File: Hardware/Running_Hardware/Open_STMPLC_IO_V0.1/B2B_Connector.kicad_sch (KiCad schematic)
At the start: 6 parts, among them J39 10144517-041802LF, J41 10144517-041802LF, J42 10144517-041802LF, J43 Screw_Terminal_01x02

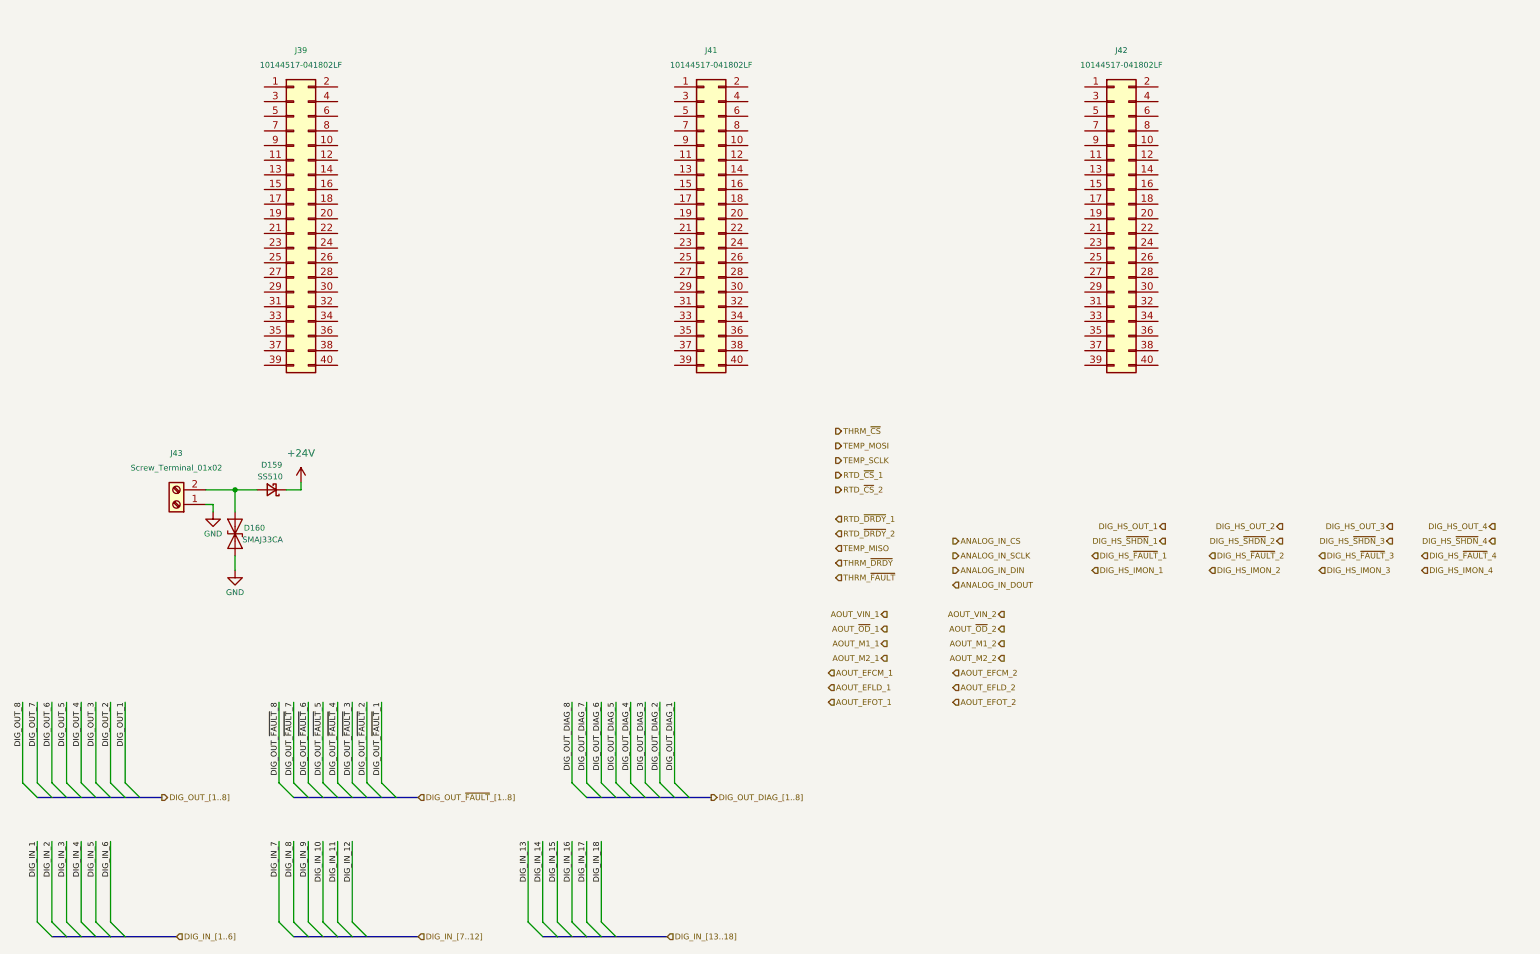
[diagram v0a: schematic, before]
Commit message: Common GND terminal changes
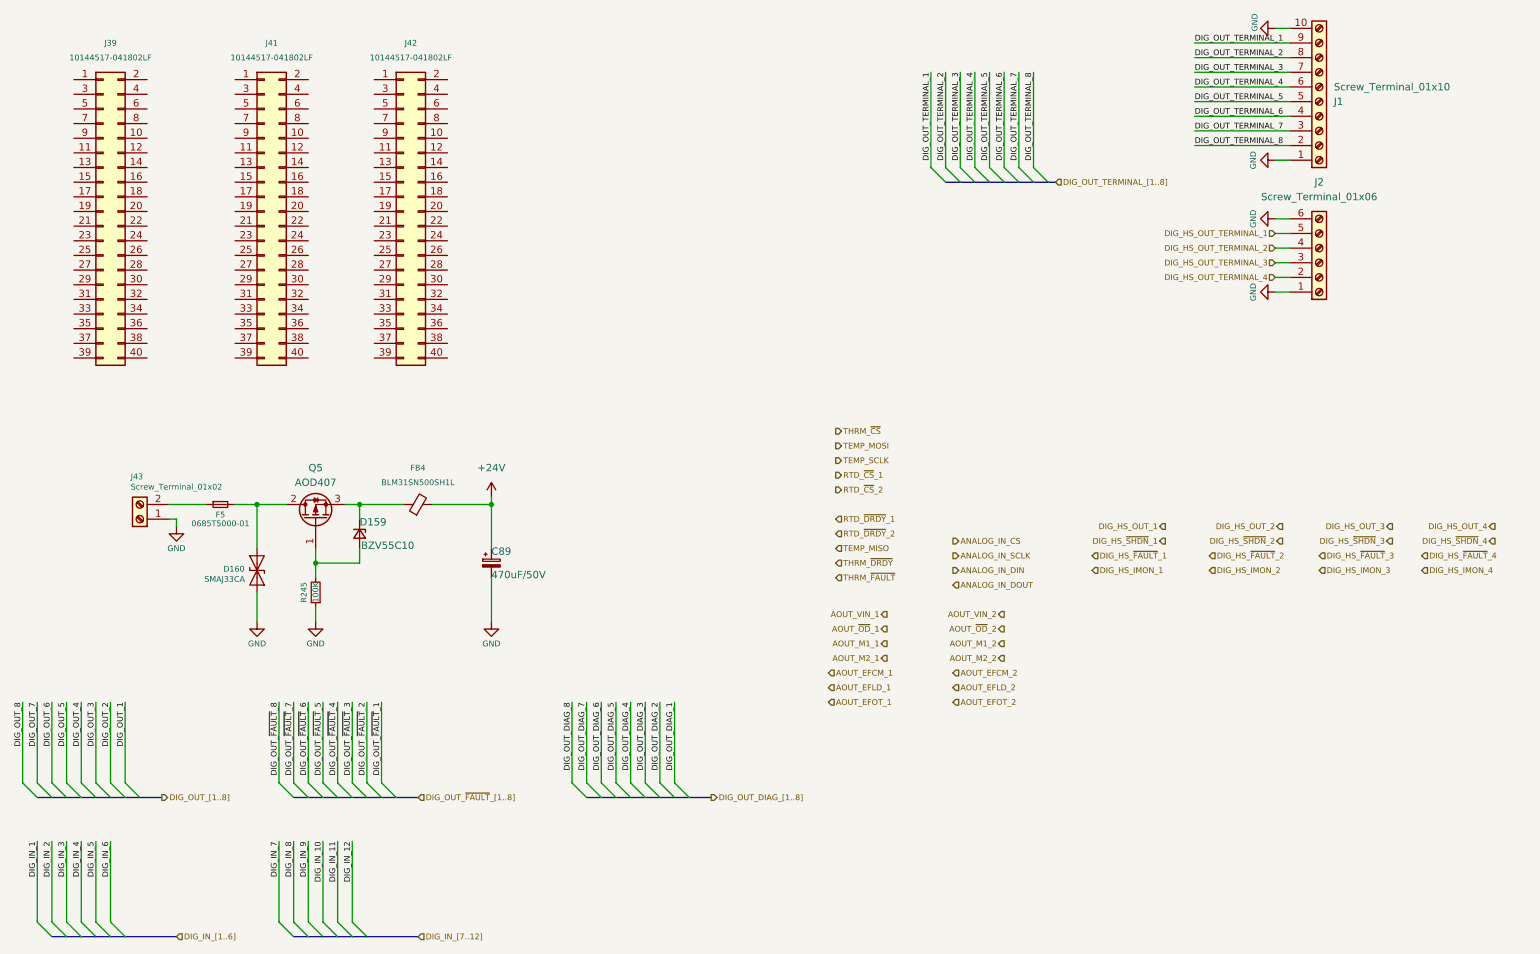
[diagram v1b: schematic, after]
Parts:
- removed D159: SS510, Diode_SMD:D_SMA, symbol Device:D_Schottky_Small
- added C89: 470uF/50V, Capacitor_THT:CP_Radial_D10.0mm_P5.00mm, symbol Device:C_Polarized_Small
- added D159: BZV55C10, Diode_SMD:D_MiniMELF, symbol Device:D_Zener_Small
- added F5: 0685T5000-01, Fuse:Fuse_1206_3216Metric, symbol Device:Fuse_Small
- added FB4: BLM31SN500SH1L, Inductor_SMD:L_1206_3216Metric_Pad1.22x1.90mm_HandSolder, symbol Device:FerriteBead_Small
- added J1: Screw_Terminal_01x10, TerminalBlock_Phoenix:TerminalBlock_Phoenix_MKDS-1-10-3.81_1x10_P3.81mm_Horizontal, symbol Connector:Screw_Terminal_01x10
- added J2: Screw_Terminal_01x06, TerminalBlock_Phoenix:TerminalBlock_Phoenix_MKDS-1-6-3.81_1x06_P3.81mm_Horizontal, symbol Connector:Screw_Terminal_01x06
- added Q5: AOD407, Package_TO_SOT_SMD:TO-252-3_TabPin2, symbol Transistor_FET:Q_PMOS_GDS
- added R245: 100K, Resistor_SMD:R_0603_1608Metric_Pad0.98x0.95mm_HandSolder, symbol Device:R_Small
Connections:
- net +24V: now also C89.1, FB4.2
- net GND: now also C89.2, J1.1 (Pin_1), J1.10 (Pin_10), J2.1 (Pin_1), J2.6 (Pin_6), R245.1
- net at J43.2 (Pin_2): now also F5.1; no longer D160.1 (A1)
- new net: D160.1 (A1), F5.2, Q5.2 (D)
- new net: D159.2 (A), Q5.1 (G), R245.2
- new net: D159.1 (K), FB4.1, Q5.3 (S)
- new net DIG_HS_OUT_TERMINAL_1: J2.5 (Pin_5)
- new net DIG_HS_OUT_TERMINAL_2: J2.4 (Pin_4)
- new net DIG_HS_OUT_TERMINAL_3: J2.3 (Pin_3)
- new net DIG_HS_OUT_TERMINAL_4: J2.2 (Pin_2)
- new net DIG_OUT_TERMINAL_1: J1.9 (Pin_9)
- new net DIG_OUT_TERMINAL_2: J1.8 (Pin_8)
- new net DIG_OUT_TERMINAL_3: J1.7 (Pin_7)
- new net DIG_OUT_TERMINAL_4: J1.6 (Pin_6)
- new net DIG_OUT_TERMINAL_5: J1.5 (Pin_5)
- new net DIG_OUT_TERMINAL_6: J1.4 (Pin_4)
- new net DIG_OUT_TERMINAL_7: J1.3 (Pin_3)
- new net DIG_OUT_TERMINAL_8: J1.2 (Pin_2)
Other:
- moved on the sheet: D160, J39, J41, J42, J43

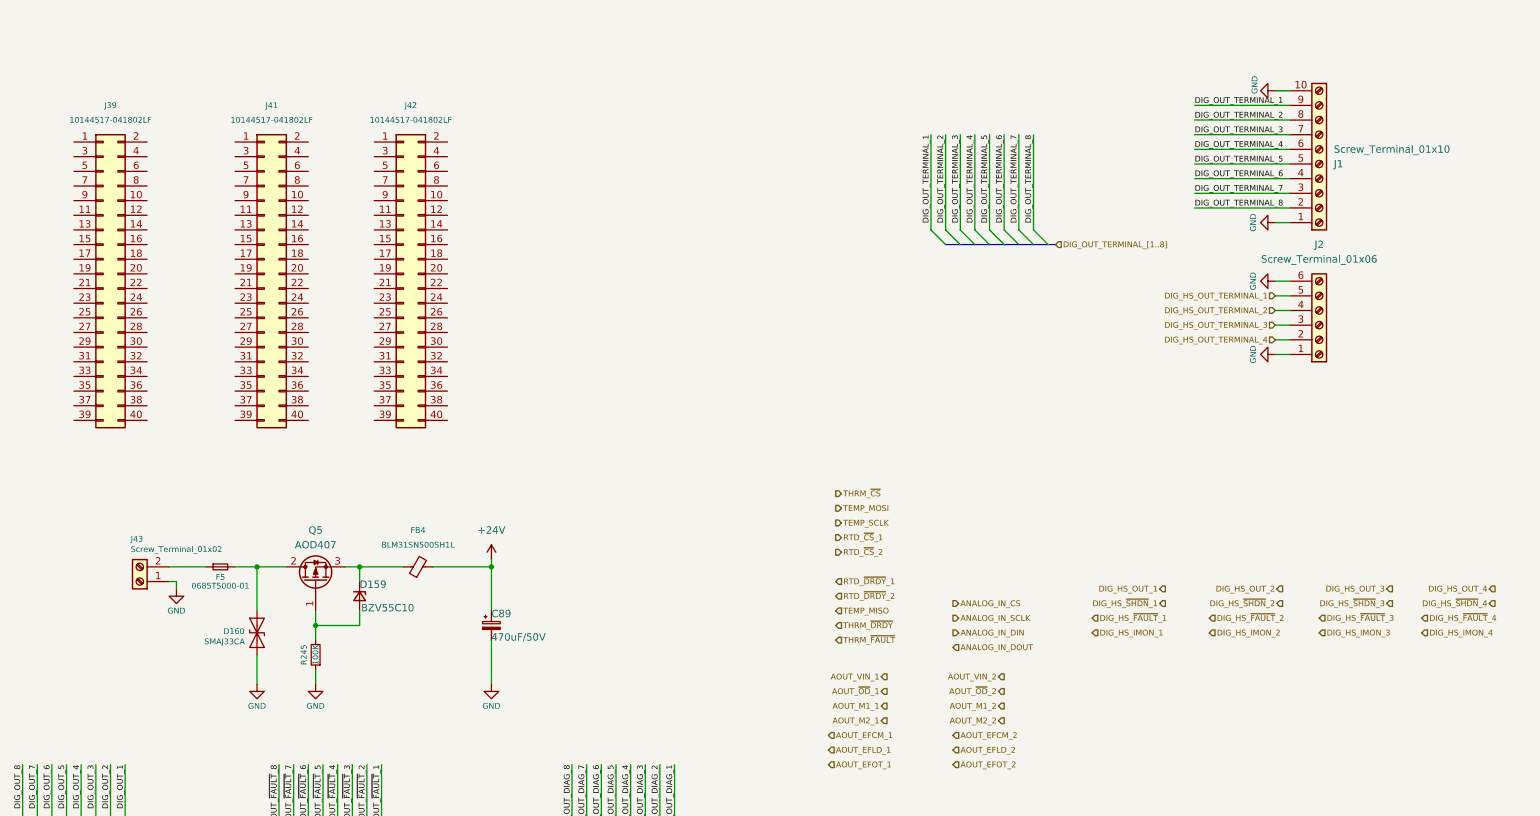
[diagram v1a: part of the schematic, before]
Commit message: Input circuit added
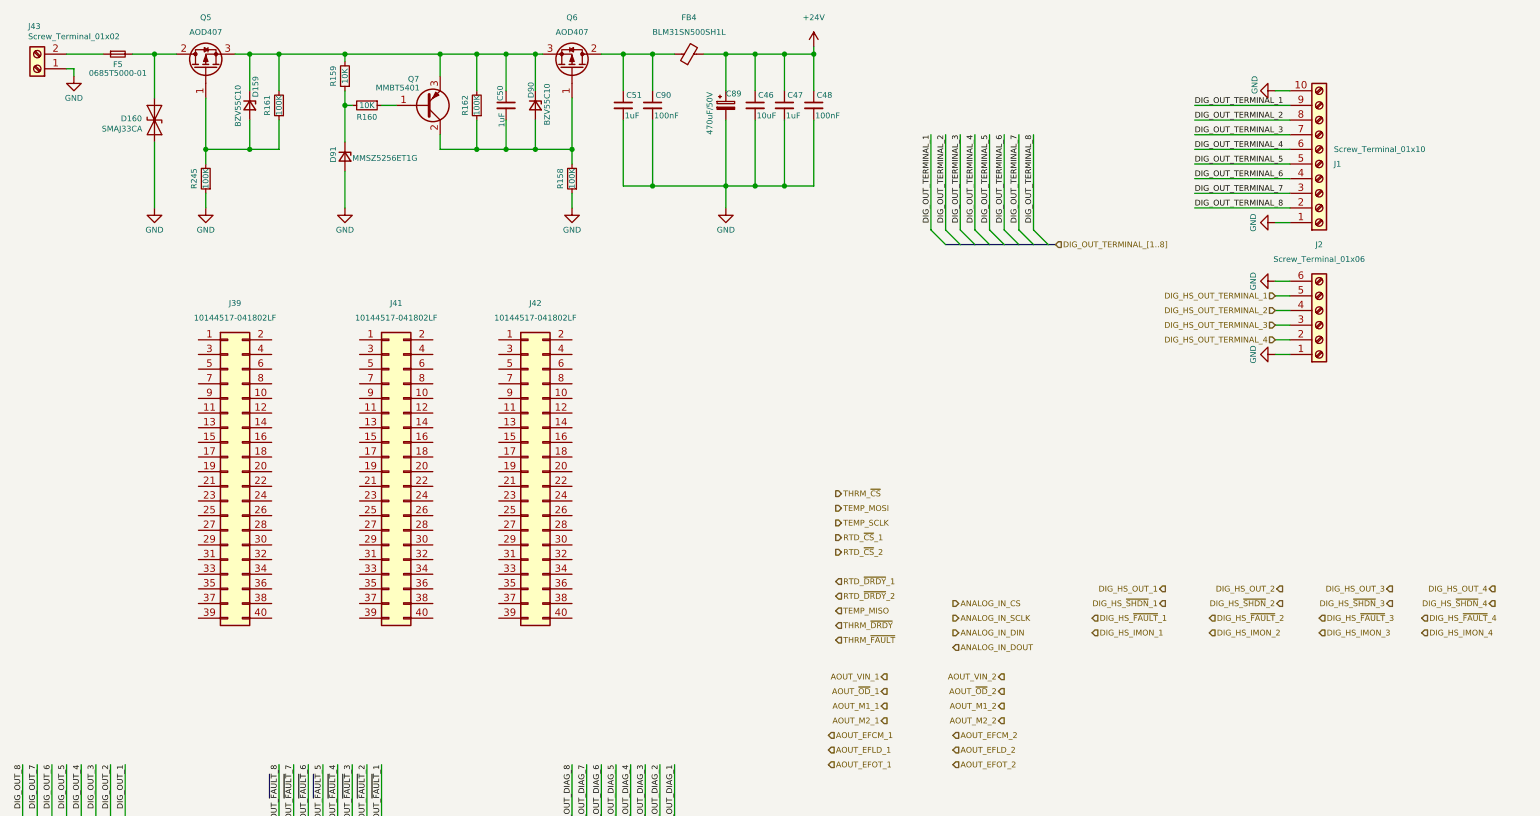
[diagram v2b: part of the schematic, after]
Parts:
- added C46: 10uF, Capacitor_SMD:C_0805_2012Metric_Pad1.18x1.45mm_HandSolder, symbol Device:C_Small
- added C47, C50, C51: 1uF, Capacitor_SMD:C_0603_1608Metric_Pad1.08x0.95mm_HandSolder, symbol Device:C_Small
- added C48, C90: 100nF, Capacitor_SMD:C_0603_1608Metric_Pad1.08x0.95mm_HandSolder, symbol Device:C_Small
- added D90: BZV55C10, Diode_SMD:D_MiniMELF, symbol Device:D_Zener_Small
- added D91: MMSZ5256ET1G, Diode_SMD:D_MiniMELF, symbol Device:D_Zener_Small
- added Q6: AOD407, Package_TO_SOT_SMD:TO-252-3_TabPin2, symbol Transistor_FET:Q_PMOS_GDS
- added Q7: MMBT5401, symbol Transistor_BJT:Q_PNP_BCE
- added R158, R161, R162: 100K, Resistor_SMD:R_0603_1608Metric_Pad0.98x0.95mm_HandSolder, symbol Device:R_Small
- added R159, R160: 10K, Resistor_SMD:R_0603_1608Metric_Pad0.98x0.95mm_HandSolder, symbol Device:R_Small
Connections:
- net +24V: now also C46.1, C47.1, C48.1
- net GND: now also C46.2, C47.2, C48.2, C51.2, C90.2, D91.2 (A), R158.1
- net at D159.2 (A), Q5.1 (G), R245.2: now also R161.1
- net at D159.1 (K), Q5.3 (S): now also C50.1, D90.1 (K), Q6.3 (S), Q7.3 (E), R159.2, R161.2, R162.2; no longer FB4.1
- new net: C51.1, C90.1, FB4.1, Q6.2 (D)
- new net: C50.2, D90.2 (A), Q6.1 (G), Q7.2 (C), R158.2, R162.1
- new net: Q7.1 (B), R160.1
- new net: D91.1 (K), R159.1, R160.2
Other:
- moved on the sheet: C89, D159, D160, F5, FB4, J39, J41, J42, J43, Q5, R245

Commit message: IO board layout
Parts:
- Q7: footprint (none) -> Package_TO_SOT_SMD:SOT-23
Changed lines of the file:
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@@
 			)
 		)
-		(property "Footprint" ""
+		(property "Footprint" "Package_TO_SOT_SMD:SOT-23"
 			(at 91.44 36.83 0)
 			(effects

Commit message: IO board layout 1
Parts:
- C89: value 470uF/50V -> 220uF/50V; footprint Capacitor_THT:CP_Radial_D10.0mm_P5.00mm -> Capacitor_SMD:CP_Elec_10x10.5
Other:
- moved on the sheet: C46, C48
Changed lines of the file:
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@@
 	(symbol
 		(lib_id "Device:C_Small")
-		(at 153.67 34.29 0)
+		(at 143.51 34.29 0)
 		(unit 1)
 		(exclude_from_sim no)
@@
 		(dnp no)
 		(property "Reference" "C48"
-			(at 154.178 32.512 0)
+			(at 144.018 32.512 0)
 			(effects
 				(font
@@
 		)
 		(property "Value" "100nF"
-			(at 153.924 36.068 0)
+			(at 143.764 36.068 0)
 			(effects
 				(font
@@
 		)
 		(property "Footprint" "Capacitor_SMD:C_0603_1608Metric_Pad1.08x0.95mm_HandSolder"
-			(at 153.67 34.29 0)
+			(at 143.51 34.29 0)
 			(effects
 				(font
@@
 		)
 		(property "Datasheet" "~"
-			(at 153.67 34.29 0)
+			(at 143.51 34.29 0)
 			(effects
 				(font
@@
 		)
 		(property "Description" "Unpolarized capacitor, small symbol"
-			(at 153.67 34.29 0)
+			(at 143.51 34.29 0)
 			(effects
 				(font
@@
 			)
 		)
-		(property "Value" "470uF/50V"
+		(property "Value" "220uF/50V"
 			(at 135.636 39.37 90)
 			(effects
@@
 			)
 		)
-		(property "Footprint" "Capacitor_THT:CP_Radial_D10.0mm_P5.00mm"
+		(property "Footprint" "Capacitor_SMD:CP_Elec_10x10.5"
 			(at 138.43 34.29 0)
 			(effects
@@
 	(symbol
 		(lib_id "Device:C_Small")
-		(at 143.51 34.29 0)
+		(at 153.67 34.29 0)
 		(unit 1)
 		(exclude_from_sim no)
@@
 		(dnp no)
 		(property "Reference" "C46"
-			(at 144.018 32.512 0)
+			(at 154.178 32.512 0)
 			(effects
 				(font
@@
 		)
 		(property "Value" "10uF"
-			(at 143.764 36.068 0)
+			(at 153.924 36.068 0)
 			(effects
 				(font
@@
 		)
 		(property "Footprint" "Capacitor_SMD:C_0805_2012Metric_Pad1.18x1.45mm_HandSolder"
-			(at 143.51 34.29 0)
+			(at 153.67 34.29 0)
 			(effects
 				(font
@@
 		)
 		(property "Datasheet" "~"
-			(at 143.51 34.29 0)
+			(at 153.67 34.29 0)
 			(effects
 				(font
@@
 		)
 		(property "Description" "Unpolarized capacitor, small symbol"
-			(at 143.51 34.29 0)
-			(effects
-				(font
+			(at 153.67 34.29 0)
+			(effects
+				(font

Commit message: LED arrengements
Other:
- moved on the sheet: C50, D159, D160, D90, D91, J43, Q7, R159, R160, R161, R162, R245

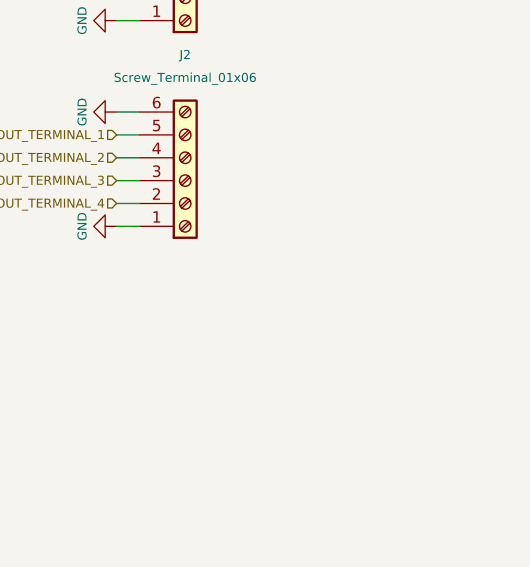
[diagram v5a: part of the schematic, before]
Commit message: Component placement IO board
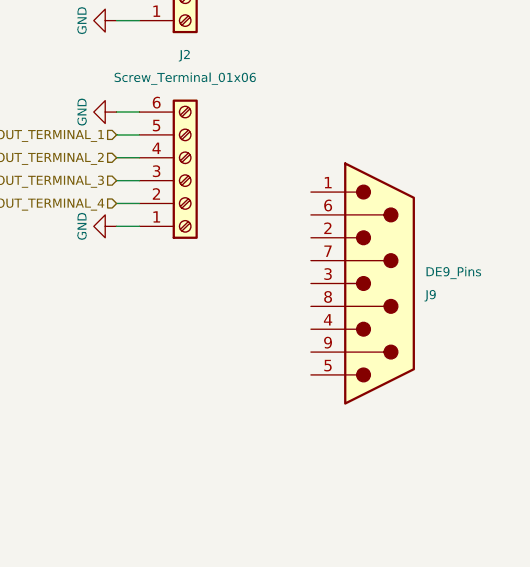
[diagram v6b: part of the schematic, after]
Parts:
- added J9: DE9_Pins, A-DF_09_PP_Z:A-DF_09_PP_Z, symbol Connector:DE9_Pins
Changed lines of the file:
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@@
+	)
+	(symbol
+		(lib_id "Connector:DE9_Pins")
+		(at 262.89 83.82 0)
+		(mirror x)
+		(unit 1)
+		(exclude_from_sim no)
+		(in_bom yes)
+		(on_board yes)
+		(dnp no)
+		(property "Reference" "J9"
+			(at 267.97 85.0901 0)
+			(effects
+				(font
+					(size 1 1)
+				)
+				(justify left)
+			)
+		)
+		(property "Value" "DE9_Pins"
+			(at 267.97 82.5501 0)
+			(effects
+				(font
+					(size 1 1)
+				)
+				(justify left)
+			)
+		)
+		(property "Footprint" "A-DF_09_PP_Z:A-DF_09_PP_Z"
+			(at 262.89 83.82 0)
+			(effects
+				(font
+					(size 1.27 1.27)
+				)
+				(hide yes)
+			)
+		)
+		(property "Datasheet" "~"
+			(at 262.89 83.82 0)
+			(effects
+				(font
+					(size 1.27 1.27)
+				)
+				(hide yes)
+			)
+		)
+		(property "Description" "9-pin D-SUB connector, pins (male)"
+			(at 262.89 83.82 0)
+			(effects
+				(font
+					(size 1.27 1.27)
+				)
+				(hide yes)
+			)
+		)
+		(pin "1"
+		)
+		(pin "9"
+		)
+		(pin "7"
+		)
+		(pin "4"
+		)
+		(pin "2"
+		)
+		(pin "3"
+		)
+		(pin "6"
+		)
+		(pin "5"
+		)
+		(pin "8"
+		)
+		(instances
+			(project "Open_STMPLC_IO_V0.1"
+				(path "/4d6787b6-1f4f-4098-b70b-d936e584350b/a733cf34-8e21-45d4-b50a-3a23f16c67a7"
+					(reference "J9")
+					(unit 1)
+				)
+			)
+		)
 	)
 	(symbol

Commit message: IO board layout
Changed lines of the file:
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@@
+		)
+	)
+	(hierarchical_label "ANALOG_IN_ERROR"
+		(shape input)
+		(at 177.8 118.11 0)
+		(effects
+			(font
+				(size 1 1)
+			)
+			(justify left)
 		)
 	)
